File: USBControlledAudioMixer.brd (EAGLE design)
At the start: 43 x 40 mm, 54 parts, among them IC1 TDA7448, IC2 TS912, IC3 MEGA8-AI, J2 AVR_SPI_PRG_6NS, Q1 16MHz, U1 LMR62014

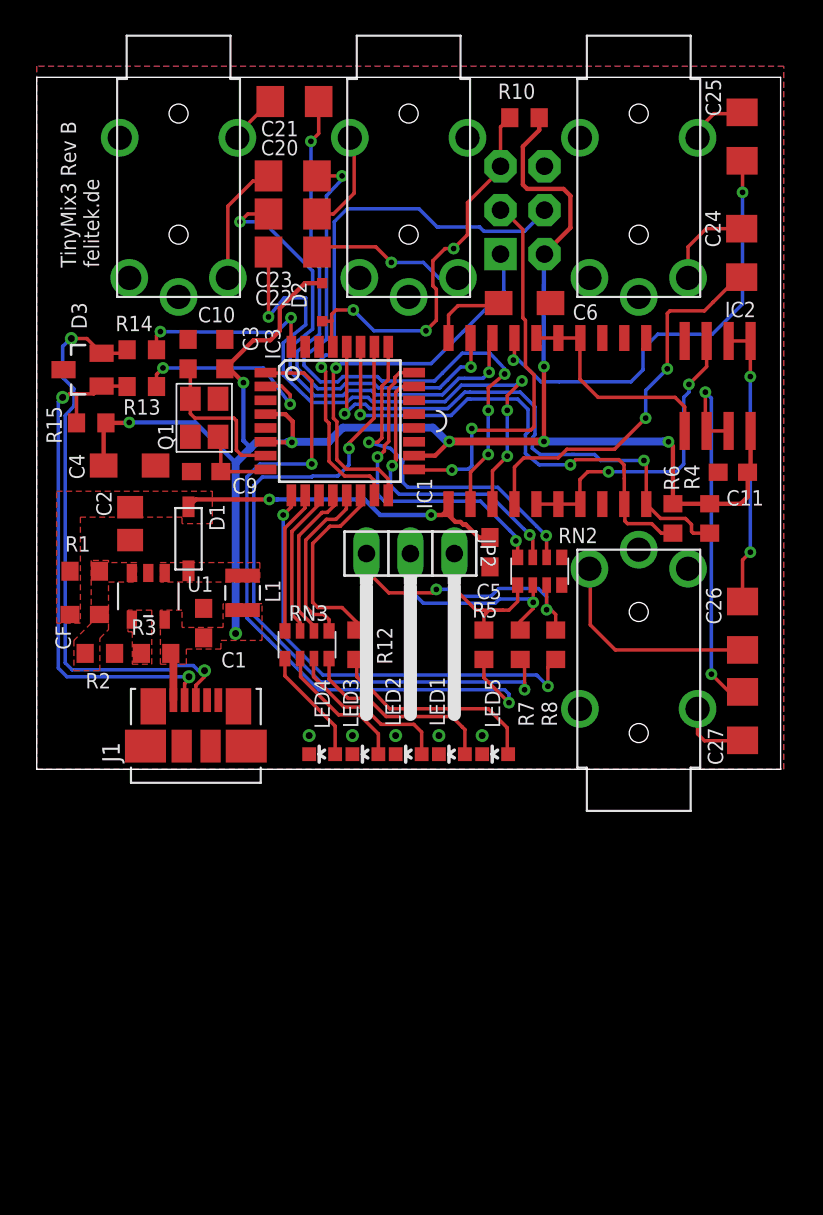
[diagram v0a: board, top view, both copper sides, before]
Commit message: Fixed audio mixing
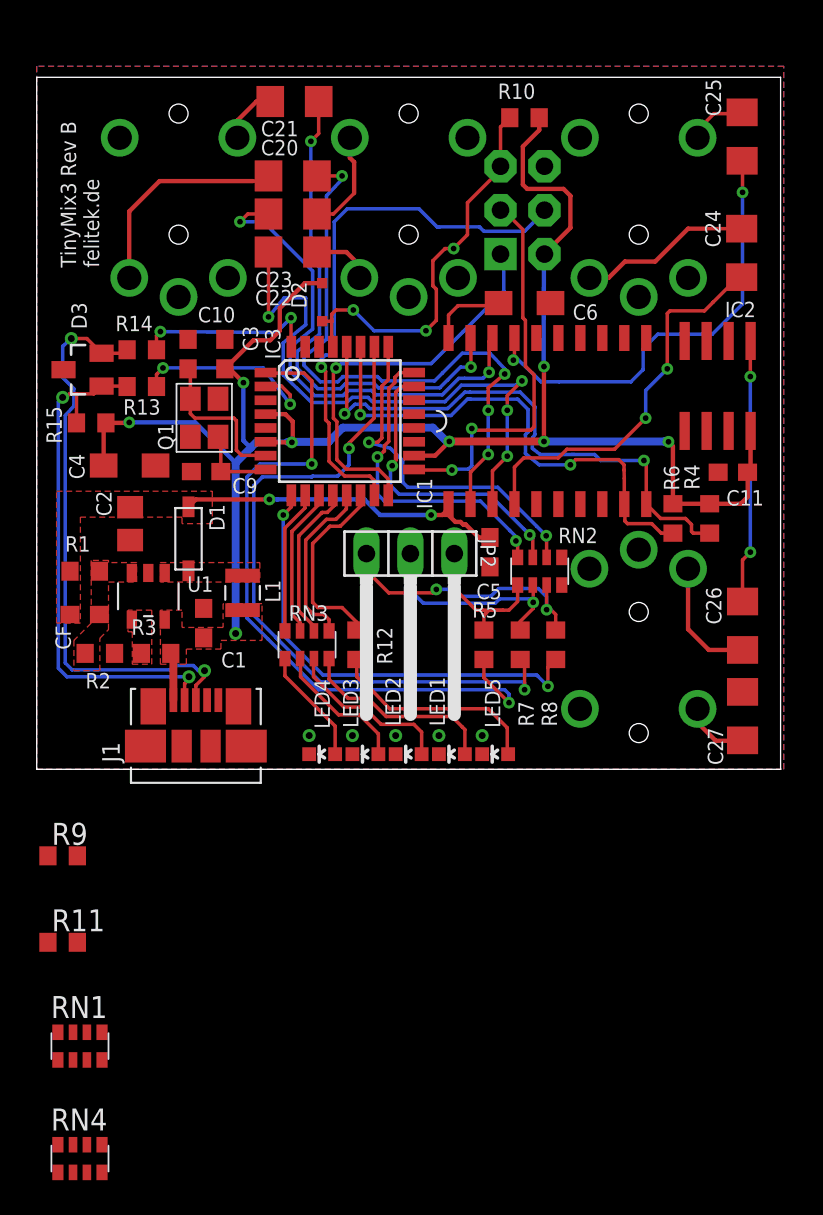
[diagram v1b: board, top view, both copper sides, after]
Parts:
- added R11, R9: 10k, rcl:R0603
- added RN1, RN4: 10k, Simplex-rlc:YC164
- IC2: value TS912 -> TS922
- flipped IN1 to the bottom
- flipped IN2 to the bottom
- flipped IN3 to the bottom
- flipped U$5 to the bottom
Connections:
- removed net N$100: C27.1, IC2.6, IC2.7
- removed net N$24: C26.1, IC2.1, IC2.2
- removed net OUT_L: IC1.5, IC1.6, IC1.7, IC2.3
- removed net OUT_R: IC1.14, IC1.15, IC1.16, IC2.5
- new net 4.5V: IC2.3, IC2.5, R11.1, R9.2
- new net FB_RES_L: C26.1, IC2.1, RN1.8
- new net FB_RES_R: C27.1, IC2.7, RN4.1
- new net MIX_IN_L: IC2.2, RN1.1, RN1.2, RN1.3, RN1.4
- new net MIX_IN_R: IC2.6, RN4.5, RN4.6, RN4.7, RN4.8
- new net N$21: IC1.5, RN1.5
- new net N$22: IC1.6, RN1.6
- new net N$25: IC1.7, RN1.7
- new net N$27: IC1.16, RN4.4
- new net N$28: IC1.15, RN4.3
- new net N$29: IC1.14, RN4.2
- net +5V: no longer C11.1, IC2.8
- net +9V: now also C11.1, IC2.8, R9.1
- net GND: now also IN1.6, IN2.6, IN3.6, R11.2; no longer IN1.2, IN2.2, IN3.2
- net N$10: now also IN3.2; no longer IN3.6
- net N$14: now also IN2.2; no longer IN2.6
- net N$16: now also IN1.2; no longer IN1.6
- net N$23: now also U$5.2; no longer U$5.6
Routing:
- net N$100: track 22.2 -> 0.00 mm, vias 2 -> 0
- net OUT_L: track 18.0 -> 0.00 mm, vias 2 -> 0
- net N$24: track 16.5 -> 0.00 mm, vias 2 -> 0
- net FB_RES_L: track 0.00 -> 15.3 mm, vias 0 -> 2
- net OUT_R: track 13.0 -> 0.00 mm
- net N$16: track 7.22 -> 12.7 mm
- net N$23: track 12.7 -> 7.14 mm
- net N$14: track 9.02 -> 3.51 mm, vias 1 -> 0
- net N$10: track 5.33 -> 9.98 mm
- net +5V: track 104.9 -> 102.5 mm
- net +9V: track 19.2 -> 21.7 mm

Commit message: Routed new mixer
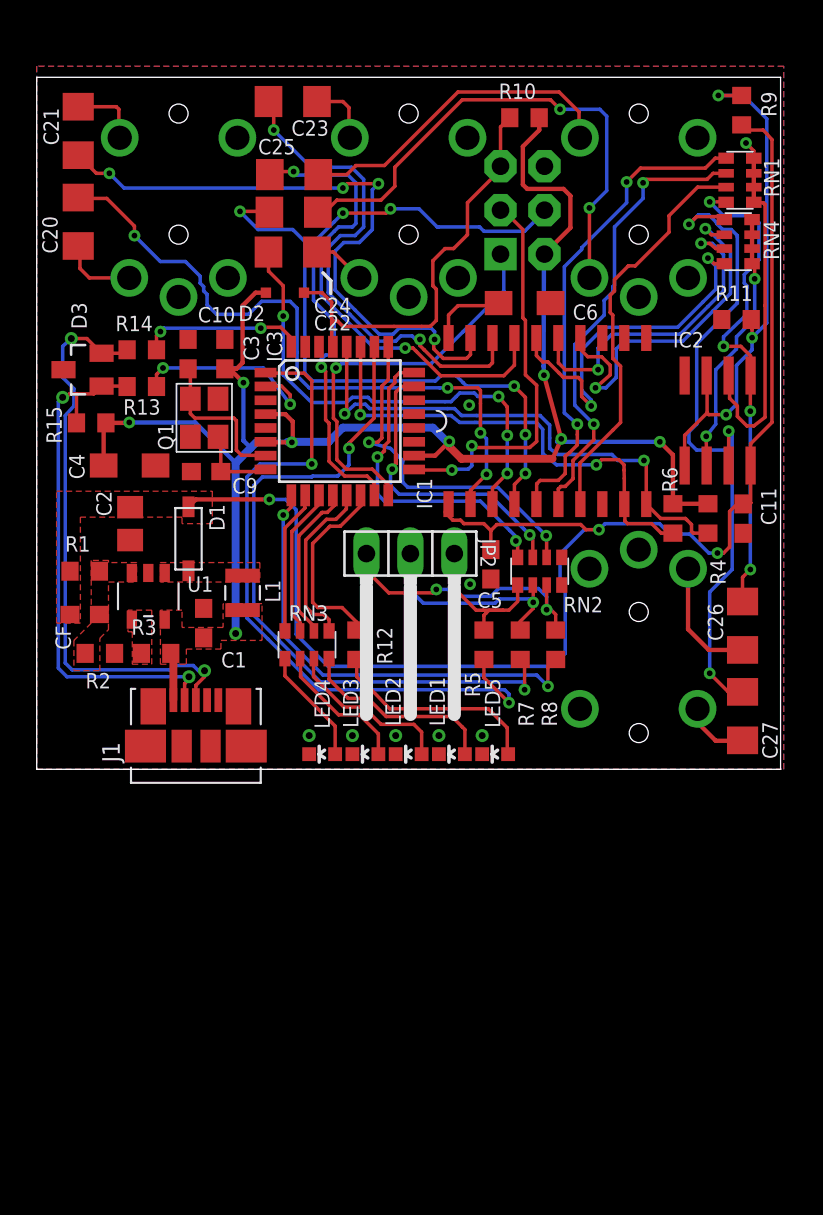
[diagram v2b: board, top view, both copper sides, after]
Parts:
- moved RN4 65.2 mm to (41.5, 30.5), turned to 270 degrees
- moved RN1 62.9 mm to (41.6, 34.0), turned to 90 degrees
- moved R9 58.3 mm to (41.8, 38.1), turned to 90 degrees
- moved R11 53.0 mm to (41.5, 26.0), turned to 180 degrees
- moved C24 26.0 mm to (15.8, 32.2), turned to 180 degrees
- moved C25 26.0 mm to (15.9, 34.4), turned to 180 degrees
- moved C20 12.7 mm to (3.40, 31.6), turned to 90 degrees
- moved C21 12.6 mm to (3.40, 36.9), turned to 270 degrees
- moved C23 6.50 mm to (15.8, 38.6)
- moved C11 2.74 mm to (41.8, 14.5), turned to 270 degrees
- moved D2 2.22 mm to (15.3, 27.6), turned to 0 degrees
- moved IC2 2.00 mm to (40.4, 20.2)
- moved C5 0.70 mm to (27.2, 11.8)
- moved R4 0.10 mm to (39.8, 14.5)
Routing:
- net +9V: track 21.7 -> 87.2 mm, vias 2 -> 3
- net FB_RES_R: track 0.00 -> 40.8 mm, vias 0 -> 3
- net 4.5V: track 0.00 -> 30.7 mm, vias 0 -> 3
- net N$21: track 0.00 -> 28.4 mm, vias 0 -> 2
- net N$22: track 0.00 -> 26.8 mm, vias 0 -> 2
- net N$25: track 0.00 -> 23.5 mm
- net N$27: track 0.00 -> 21.6 mm, vias 0 -> 2
- net MIX_IN_L: track 0.00 -> 21.2 mm, vias 0 -> 1
- net N$29: track 0.00 -> 21.1 mm, vias 0 -> 2
- net N$10: track 9.98 -> 30.2 mm, vias 0 -> 2
- net N$28: track 0.00 -> 18.9 mm, vias 0 -> 2
- net N$12: track 3.44 -> 19.0 mm
- net MIX_IN_R: track 0.00 -> 15.4 mm, vias 0 -> 2
- net FB_RES_L: track 15.3 -> 28.6 mm, vias 2 -> 4
- net IN_3_L: track 22.6 -> 33.8 mm, vias 2 -> 4
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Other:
- board text added: "TinyMix3 Rev C felitek.de"
- board text removed: "TinyMix3 Rev B felitek.de"
